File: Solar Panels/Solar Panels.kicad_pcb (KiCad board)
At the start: 2 copper layers, 113 x 82 mm, 75 parts, among them J2 5040500891

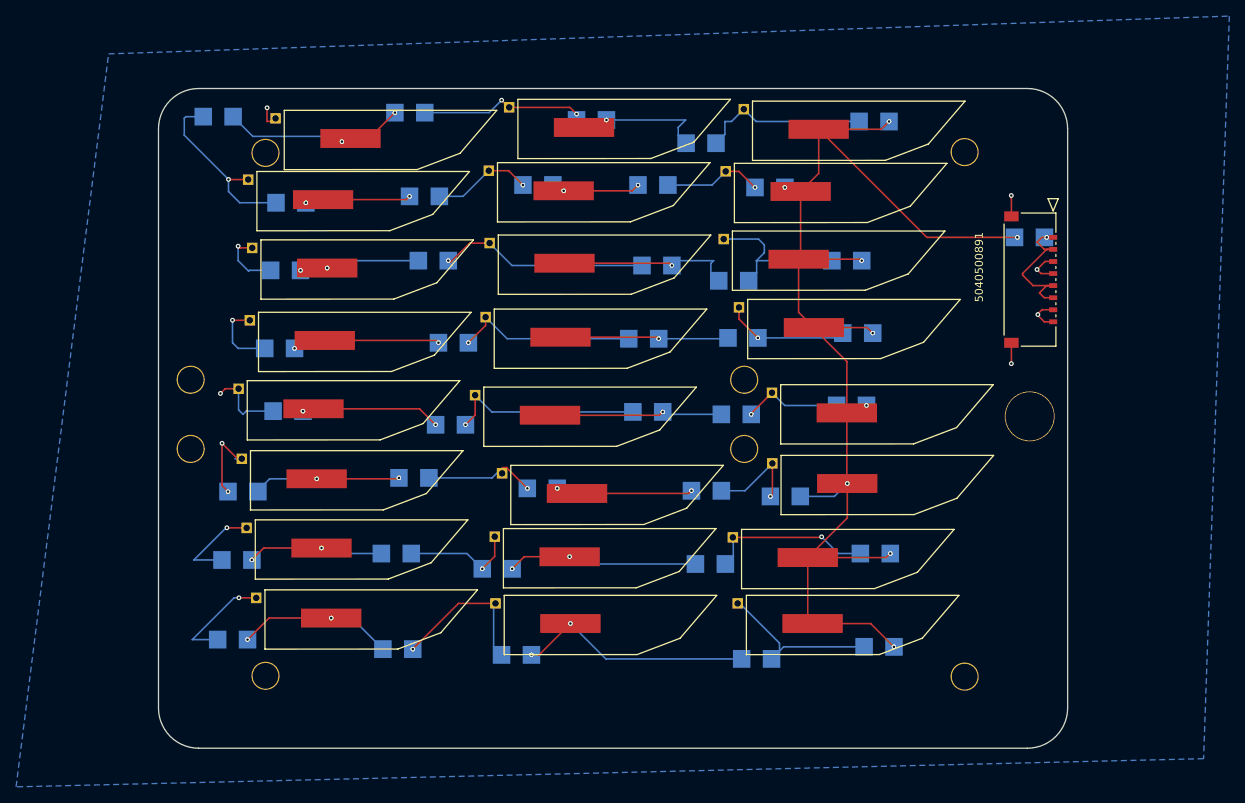
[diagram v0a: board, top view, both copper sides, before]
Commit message: Initial Panels Revision
Changed the Solar Panels to adjust to structural needs.
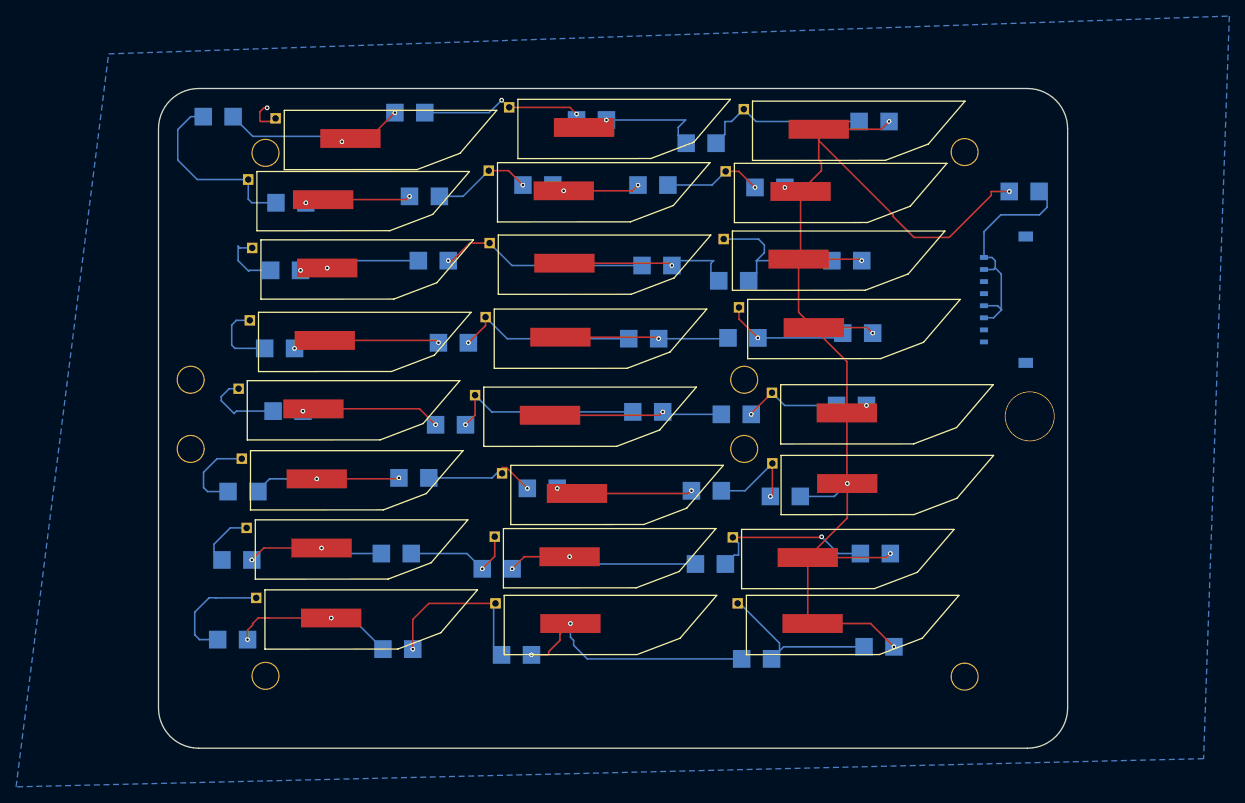
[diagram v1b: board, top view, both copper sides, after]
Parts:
- J2: moved to B.Cu
- moved J2 8.96 mm to (177.6, 96.0)
- moved CR3 5.74 mm to (182.6, 87.8)
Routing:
- net GND: track 102.9 -> 88.3 mm, vias 13 -> 1
- net +VDC: track 18.3 -> 29.2 mm, vias 1 -> 0
- net Net-(U1-+): track 155.4 -> 158.3 mm
- net Net-(U23--): track 19.5 -> 21.7 mm
- net Net-(U23-+): track 29.6 -> 31.6 mm
- net Net-(U19--): track 20.5 -> 21.3 mm
- net Net-(U24-+): track 19.5 -> 20.4 mm

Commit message: Updated Solar Panels
Revised to fit Brett's preferences.
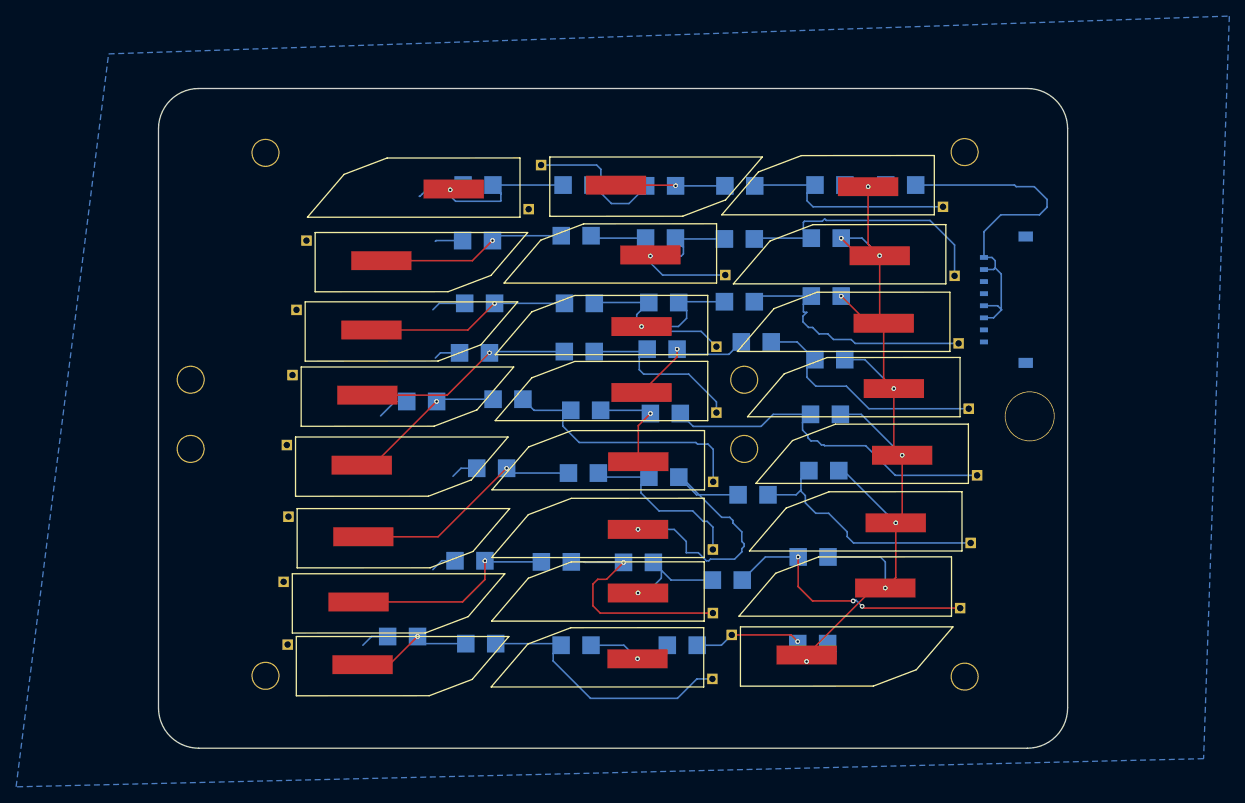
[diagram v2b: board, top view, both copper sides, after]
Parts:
- moved CR6 33.4 mm to (114.7, 87.0)
- moved CR31 31.0 mm to (116.4, 122.2)
- moved CR36 29.0 mm to (113.7, 133.7)
- moved CR16 24.5 mm to (114.9, 101.7)
- moved CR21 24.2 mm to (114.3, 107.9)
- moved CR11 23.7 mm to (114.7, 93.9)
- moved CR2 22.8 mm to (127.1, 87.0)
- moved CR41 21.1 mm to (105.3, 143.1)
- moved CR28 21.1 mm to (127.8, 122.8)
- moved CR33 19.9 mm to (124.5, 133.8)
- moved CR8 19.5 mm to (126.9, 93.3)
- moved CR13 18.9 mm to (127.3, 101.7)
- moved CR35 17.6 mm to (134.7, 133.9)
- moved CR26 16.7 mm to (107.7, 113.9)
- moved CR10 16.6 mm to (137.4, 93.6)
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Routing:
- net GND: track 88.3 -> 31.2 mm, vias 1 -> 0
- net Net-(U13--): track 12.4 -> 44.0 mm, vias 1 -> 0
- net Net-(U1-+): track 158.3 -> 134.3 mm
- net Net-(U3--): track 12.4 -> 33.7 mm, vias 1 -> 0
- net Net-(U23-+): track 31.6 -> 11.0 mm, vias 2 -> 1
- net Net-(U17-+): track 17.1 -> 37.6 mm, vias 2 -> 1
- net Net-(U16--): track 12.0 -> 31.9 mm, vias 1 -> 0
- net +VDC: track 29.2 -> 44.9 mm
- net Net-(U20--): track 14.3 -> 29.4 mm
- net Net-(U10--): track 15.6 -> 30.7 mm, vias 1 -> 0
- net Net-(U7--): track 20.0 -> 32.0 mm
- net Net-(U19--): track 21.3 -> 33.2 mm, vias 1 -> 3
- net Net-(U23--): track 21.7 -> 33.3 mm, vias 1 -> 0
- net Net-(U18-+): track 18.3 -> 29.3 mm, vias 2 -> 1
- net Net-(U6-+): track 13.2 -> 23.6 mm, vias 2 -> 1
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
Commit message: Modifications For 2U Panels
Made structural modifications to suit Brett's structure and tried to improve the PCB board based on Parker's suggestions. Schematic is extremely wonky right now but will try to fix it ASAP.
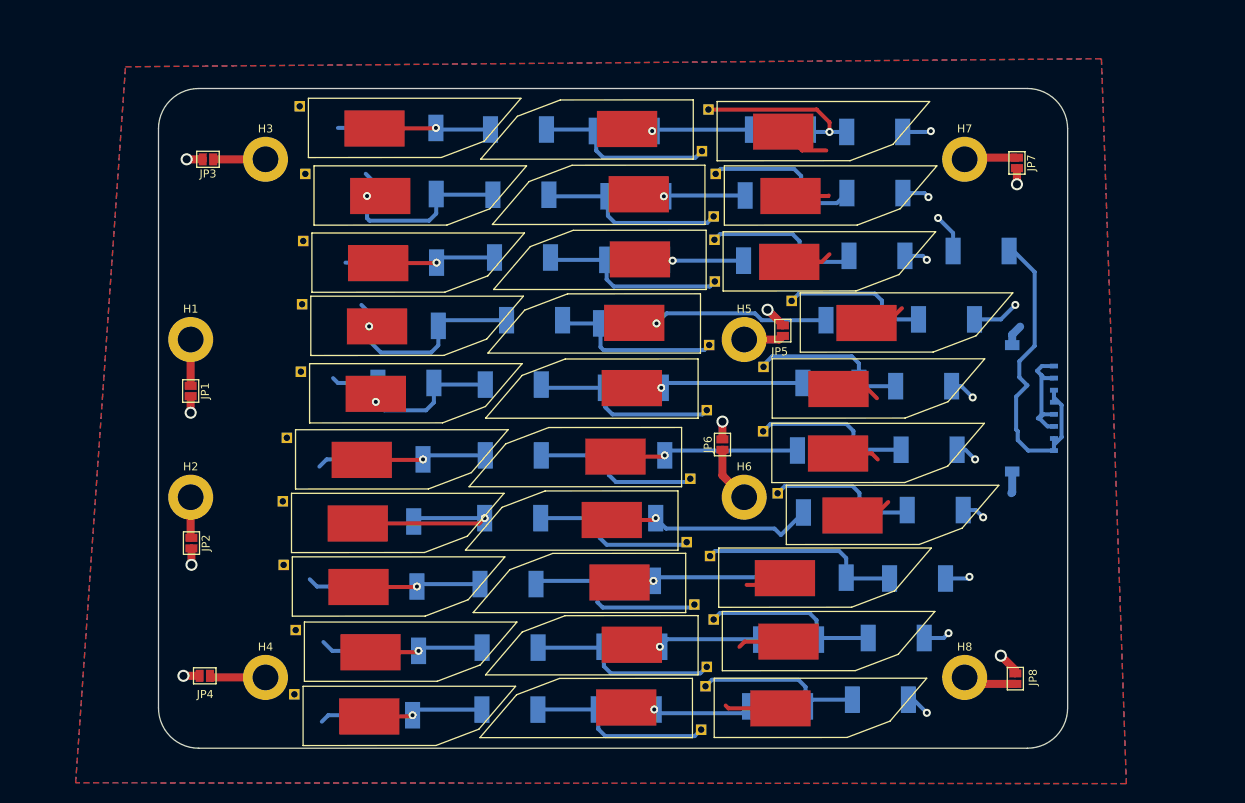
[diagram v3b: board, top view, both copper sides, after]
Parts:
- removed 3.2 (x2): 3.2 hole, Calgary2Space:3.2 hole
- removed ? (x6): , 
- removed REF**: 6 hole, Calgary2Space:6 hole
- removed U1, U10, U11, U12, U13, U14, U15, U16, U17, U18, U19, U2, U20, U21, U22, U23, U24, U3, U4, U5, U6, U7, U8, U9: ~, Calgary2Space:TrisolX Solar Wings
- added CR42: S3B_R1_00001, Solar Panel Library:SMC&slash_DO-214AB_PNJ, B.Cu at (153.3, 143.5)
- added CR43: S3B_R1_00001, Solar Panel Library:SMC&slash_DO-214AB_PNJ, B.Cu at (118.7, 144.5)
- added CR44: S3B_R1_00001, Solar Panel Library:SMC&slash_DO-214AB_PNJ, B.Cu at (166.7, 143.3)
- added CR45: S3B_R1_00001, Solar Panel Library:SMC&slash_DO-214AB_PNJ, B.Cu at (133.8, 144.4)
- added CR46: S3B_R1_00001, Solar Panel Library:SMC&slash_DO-214AB_PNJ, B.Cu at (103.8, 144.9)
- added CR47: S3B_R1_00001, Solar Panel Library:SMC&slash_DO-214AB_PNJ, B.Cu at (151.9, 151.8)
- added CR48: S3B_R1_00001, Solar Panel Library:SMC&slash_DO-214AB_PNJ, B.Cu at (118.7, 152.2)
- added CR49: S3B_R1_00001, Solar Panel Library:SMC&slash_DO-214AB_PNJ, B.Cu at (164.7, 151.0)
- added CR50: S3B_R1_00001, Solar Panel Library:SMC&slash_DO-214AB_PNJ, B.Cu at (133.1, 152.2)
- added CR51: S3B_R1_00001, Solar Panel Library:SMC&slash_DO-214AB_PNJ, B.Cu at (103.1, 152.9)
- added H1: MountingHole_Pad, MountingHole:MountingHole_3.2mm_M3_DIN965_Pad, F.Cu at (79.0, 106.2)
- added H2: MountingHole_Pad, MountingHole:MountingHole_3.2mm_M3_DIN965_Pad, F.Cu at (79.0, 125.8)
- added H3: MountingHole_Pad, MountingHole:MountingHole_3.2mm_M3_DIN965_Pad, F.Cu at (88.3, 83.8)
- added H4: MountingHole_Pad, MountingHole:MountingHole_3.2mm_M3_DIN965_Pad, F.Cu at (88.3, 148.2)
- added H5: MountingHole_Pad, MountingHole:MountingHole_3.2mm_M3_DIN965_Pad, F.Cu at (147.8, 106.2)
- added H6: MountingHole_Pad, MountingHole:MountingHole_3.2mm_M3_DIN965_Pad, F.Cu at (147.8, 125.8)
- added H7: MountingHole_Pad, MountingHole:MountingHole_3.2mm_M3_DIN965_Pad, F.Cu at (175.2, 83.8)
- added H8: MountingHole_Pad, MountingHole:MountingHole_3.2mm_M3_DIN965_Pad, F.Cu at (175.2, 148.2)
- added JP1: Jumper_2_Open, Jumper:SolderJumper-2_P1.3mm_Open_Pad1.0x1.5mm, F.Cu at (79.0, 112.6)
- added JP2: Jumper_2_Open, Jumper:SolderJumper-2_P1.3mm_Open_Pad1.0x1.5mm, F.Cu at (79.1, 131.5)
- added JP3: Jumper_2_Open, Jumper:SolderJumper-2_P1.3mm_Open_Pad1.0x1.5mm, F.Cu at (81.2, 83.8)
- added JP4: Jumper_2_Open, Jumper:SolderJumper-2_P1.3mm_Open_Pad1.0x1.5mm, F.Cu at (80.8, 148.0)
- added JP5: Jumper_2_Open, Jumper:SolderJumper-2_P1.3mm_Open_Pad1.0x1.5mm, F.Cu at (152.6, 105.1)
- added JP6: Jumper_2_Open, Jumper:SolderJumper-2_P1.3mm_Open_Pad1.0x1.5mm, F.Cu at (145.1, 119.2)
- added JP7: Jumper_2_Open, Jumper:SolderJumper-2_P1.3mm_Open_Pad1.0x1.5mm, F.Cu at (181.7, 84.2)
- added JP8: Jumper_2_Open, Jumper:SolderJumper-2_P1.3mm_Open_Pad1.0x1.5mm, F.Cu at (181.5, 148.3)
- added SC1: Solar_Cell, Solar Panel Library:TrisolX Solar Wings, F.Cu at (152.7, 80.1)
- added SC10: Solar_Cell, Solar Panel Library:TrisolX Solar Wings, F.Cu at (163.0, 103.9)
- added SC11: Solar_Cell, Solar Panel Library:TrisolX Solar Wings, F.Cu at (134.1, 104.4)
- added SC12: Solar_Cell, Solar Panel Library:TrisolX Solar Wings, F.Cu at (102.2, 104.3)
- added SC13: Solar_Cell, Solar Panel Library:TrisolX Solar Wings, F.Cu at (159.5, 112.1)
- added SC14: Solar_Cell, Solar Panel Library:TrisolX Solar Wings, F.Cu at (133.8, 112.5)
- added SC15: Solar_Cell, Solar Panel Library:TrisolX Solar Wings, F.Cu at (102.0, 112.7)
- added SC16: Solar_Cell, Solar Panel Library:TrisolX Solar Wings, F.Cu at (159.5, 120.1)
- added SC17: Solar_Cell, Solar Panel Library:TrisolX Solar Wings, F.Cu at (131.8, 121.0)
- added SC18: Solar_Cell, Solar Panel Library:TrisolX Solar Wings, F.Cu at (100.3, 120.9)
- added SC19: Solar_Cell, Solar Panel Library:TrisolX Solar Wings, F.Cu at (161.3, 127.8)
- added SC2: Solar_Cell, Solar Panel Library:TrisolX Solar Wings, F.Cu at (133.2, 80.3)
- added SC20: Solar_Cell, Solar Panel Library:TrisolX Solar Wings, F.Cu at (131.3, 128.9)
- added SC21: Solar_Cell, Solar Panel Library:TrisolX Solar Wings, F.Cu at (99.8, 128.8)
- added SC22: Solar_Cell, Solar Panel Library:TrisolX Solar Wings, F.Cu at (152.9, 135.6)
- added SC23: Solar_Cell, Solar Panel Library:TrisolX Solar Wings, F.Cu at (132.3, 136.6)
- added SC24: Solar_Cell, Solar Panel Library:TrisolX Solar Wings, F.Cu at (99.9, 136.7)
- added SC25: Solar_Cell, Solar Panel Library:TrisolX Solar Wings, F.Cu at (153.3, 143.5)
- added SC26: Solar_Cell, Solar Panel Library:TrisolX Solar Wings, F.Cu at (133.8, 144.4)
- added SC27: Solar_Cell, Solar Panel Library:TrisolX Solar Wings, F.Cu at (101.4, 144.8)
- added SC28: Solar_Cell, Solar Panel Library:TrisolX Solar Wings, F.Cu at (152.3, 151.8)
- added SC29: Solar_Cell, Solar Panel Library:TrisolX Solar Wings, F.Cu at (133.1, 152.2)
- added SC3: Solar_Cell, Solar Panel Library:TrisolX Solar Wings, F.Cu at (101.9, 79.7)
- added SC30: Solar_Cell, Solar Panel Library:TrisolX Solar Wings, F.Cu at (101.2, 152.8)
- added SC4: Solar_Cell, Solar Panel Library:TrisolX Solar Wings, F.Cu at (153.6, 88.1)
- added SC5: Solar_Cell, Solar Panel Library:TrisolX Solar Wings, F.Cu at (134.7, 88.4)
- added SC6: Solar_Cell, Solar Panel Library:TrisolX Solar Wings, F.Cu at (102.6, 88.1)
- added SC7: Solar_Cell, Solar Panel Library:TrisolX Solar Wings, F.Cu at (153.4, 96.3)
- added SC8: Solar_Cell, Solar Panel Library:TrisolX Solar Wings, F.Cu at (134.8, 96.5)
- added SC9: Solar_Cell, Solar Panel Library:TrisolX Solar Wings, F.Cu at (102.3, 96.5)
- CR1, CR10, CR11, CR12, CR13, CR14, CR15, CR16, CR17, CR18, CR19, CR2, CR20, CR21, CR22, CR23, CR24, CR25, CR26, CR27, CR28, CR29, CR3, CR30, CR31, CR32, CR33, CR34, CR35, CR36, CR37, CR38, CR39, CR4, CR40, CR41, CR5, CR6, CR7, CR8, CR9: value S3BB -> S3B_R1_00001; footprint Calgary2Space:SMB_DIO -> Solar Panel Library:SMC&slash_DO-214AB_PNJ
- J2: footprint Calgary2Space:5040500891 -> Solar Panel Library:5040500891
- moved CR21 58.8 mm to (172.9, 103.7)
- moved CR16 49.7 mm to (164.3, 95.8)
- moved CR38 42.7 mm to (157.0, 135.8)
- moved CR12 41.4 mm to (106.1, 96.6)
- moved CR23 40.2 mm to (158.6, 111.6)
- moved CR8 37.5 mm to (164.0, 88.0)
- moved CR2 37.5 mm to (164.0, 80.4)
- moved CR19 37.0 mm to (121.7, 103.8)
- moved CR33 34.7 mm to (158.6, 127.7)
- moved CR22 32.3 mm to (170.1, 112.0)
- moved CR20 31.4 mm to (106.3, 104.5)
- moved CR1 31.1 mm to (177.2, 95.2)
- moved CR37 30.4 mm to (169.3, 135.9)
- moved CR28 30.2 mm to (157.9, 120.0)
- moved CR32 27.3 mm to (171.5, 127.4)
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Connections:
- CR1 pad 1: Net-(U1--) -> +VDC
- CR1 pad 2: Net-(U4-+) -> Net-(SC1-+)
- CR10 pad 1: Net-(U5-+) -> Net-(SC5--)
- CR10 pad 2: Net-(U5--) -> Net-(SC6-+)
- CR11 pad 1: Net-(U6-+) -> Net-(SC6-+)
- CR12 pad 1: Net-(U7--) -> Net-(SC9-+)
- CR12 pad 2: Net-(U8-+) -> GND
- CR13 pad 1: Net-(U8--) -> Net-(SC8--)
- CR13 pad 2: Net-(U9-+) -> Net-(SC9-+)
- CR14 pad 1: Net-(U1-+) -> Net-(SC8-+)
- CR14 pad 2: Net-(U7--) -> Net-(SC8--)
- CR15 pad 1: Net-(U8-+) -> Net-(SC7--)
- CR15 pad 2: Net-(U8--) -> Net-(SC8-+)
- CR16 pad 1: Net-(U9-+) -> Net-(SC1-+)
- CR16 pad 2: GND -> Net-(SC7--)
- CR17 pad 1: Net-(U10--) -> Net-(SC10--)
- CR17 pad 2: Net-(U11-+) -> Net-(SC11-+)
- CR18 pad 1: Net-(U11--) -> Net-(SC11-+)
- CR18 pad 2: Net-(U12-+) -> Net-(SC11--)
- CR19 pad 1: Net-(U1-+) -> Net-(SC11--)
- CR19 pad 2: Net-(U10--) -> Net-(SC12-+)
- CR2 pad 1: Net-(U4--) -> Net-(SC1-+)
- CR2 pad 2: Net-(U2-+) -> Net-(SC1--)
- CR20 pad 1: Net-(U11-+) -> Net-(SC12-+)
- CR20 pad 2: Net-(U11--) -> GND
- CR21 pad 1: Net-(U12-+) -> Net-(SC1-+)
- CR21 pad 2: GND -> Net-(SC10--)
- CR22 pad 1: Net-(U13--) -> Net-(SC1-+)
- CR22 pad 2: Net-(U14-+) -> Net-(SC13--)
- CR23 pad 1: Net-(U14--) -> Net-(SC13--)
- CR23 pad 2: Net-(U15-+) -> Net-(SC14-+)
- CR24 pad 1: Net-(U1-+) -> Net-(SC14-+)
- CR24 pad 2: Net-(U13--) -> Net-(SC14--)
- CR25 pad 1: Net-(U14-+) -> Net-(SC14--)
- CR25 pad 2: Net-(U14--) -> Net-(SC15-+)
- CR26 pad 1: Net-(U15-+) -> Net-(SC15-+)
- CR27 pad 1: Net-(U16--) -> Net-(SC1-+)
- CR27 pad 2: Net-(U17-+) -> Net-(SC16--)
- CR28 pad 1: Net-(U17--) -> Net-(SC16--)
- CR28 pad 2: Net-(U18-+) -> Net-(SC17-+)
- CR29 pad 1: Net-(U1-+) -> Net-(SC17-+)
- CR29 pad 2: Net-(U16--) -> Net-(SC17--)
- CR3 pad 1: +VDC -> Net-(SC1--)
- CR3 pad 2: Net-(U1-+) -> Net-(SC2-+)
- CR30 pad 1: Net-(U17-+) -> Net-(SC17--)
- CR30 pad 2: Net-(U17--) -> Net-(SC18-+)
- CR31 pad 1: Net-(U18-+) -> Net-(SC18-+)
- CR32 pad 1: Net-(U19--) -> Net-(SC1-+)
- CR32 pad 2: Net-(U20-+) -> Net-(SC19--)
- CR33 pad 1: Net-(U20--) -> Net-(SC19--)
- CR33 pad 2: Net-(U21-+) -> Net-(SC20-+)
- CR34 pad 1: Net-(U1-+) -> Net-(SC20-+)
- CR34 pad 2: Net-(U19--) -> Net-(SC20--)
- CR35 pad 1: Net-(U20-+) -> Net-(SC20--)
- CR35 pad 2: Net-(U20--) -> Net-(SC21-+)
- CR36 pad 1: Net-(U21-+) -> Net-(SC21-+)
- CR37 pad 1: Net-(U22--) -> Net-(SC1-+)
- CR37 pad 2: Net-(U23-+) -> Net-(SC22--)
- CR38 pad 1: Net-(U23--) -> Net-(SC22--)
- CR38 pad 2: Net-(U24-+) -> Net-(SC23-+)
- CR39 pad 1: Net-(U1-+) -> Net-(SC23-+)
- CR39 pad 2: Net-(U22--) -> Net-(SC23--)
- CR4 pad 1: Net-(U1-+) -> Net-(SC2-+)
- CR4 pad 2: Net-(U1--) -> Net-(SC2--)
- CR40 pad 1: Net-(U23-+) -> Net-(SC23--)
- CR40 pad 2: Net-(U23--) -> Net-(SC24-+)
- CR41 pad 1: Net-(U24-+) -> Net-(SC24-+)
- CR5 pad 1: Net-(U4-+) -> Net-(SC2--)
- CR5 pad 2: Net-(U4--) -> Net-(SC3-+)
- CR6 pad 1: Net-(U2-+) -> Net-(SC3-+)
- CR7 pad 1: Net-(U3--) -> Net-(SC4--)
- CR7 pad 2: Net-(U5-+) -> Net-(SC5-+)
- CR8 pad 1: Net-(U5--) -> Net-(SC1-+)
- CR8 pad 2: Net-(U6-+) -> Net-(SC4--)
- CR9 pad 1: Net-(U1-+) -> Net-(SC5-+)
- CR9 pad 2: Net-(U3--) -> Net-(SC5--)
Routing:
- net Net-(U1-+): track 134.3 -> 0.00 mm, vias 9 -> 0
- net Net-(SC1-+): track 0.00 -> 94.5 mm, vias 0 -> 11
- net GND: track 31.2 -> 83.5 mm, vias 0 -> 8
- net Net-(U13--): track 44.0 -> 0.00 mm
- net Net-(U17-+): track 37.6 -> 0.00 mm, vias 1 -> 0
- net Net-(U3--): track 33.7 -> 0.00 mm
- net Net-(U23--): track 33.3 -> 0.00 mm
- net Net-(U19--): track 33.2 -> 0.00 mm, vias 3 -> 0
- net Net-(U14--): track 32.8 -> 0.00 mm
- net Net-(U7--): track 32.0 -> 0.00 mm
- net Net-(U16--): track 31.9 -> 0.00 mm
- net Net-(U10--): track 30.7 -> 0.00 mm
- net Net-(U20--): track 29.4 -> 0.00 mm, vias 1 -> 0
- net Net-(U18-+): track 29.3 -> 0.00 mm, vias 1 -> 0
- net Net-(U1--): track 27.1 -> 0.00 mm
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- added copper zone on F.Cu, net Net-(SC1-+)
